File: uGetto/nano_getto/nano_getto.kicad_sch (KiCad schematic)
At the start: 9 parts, among them J1 Conn_01x06_Male, SW1 SW_Push, U1 ATtiny13A-SS

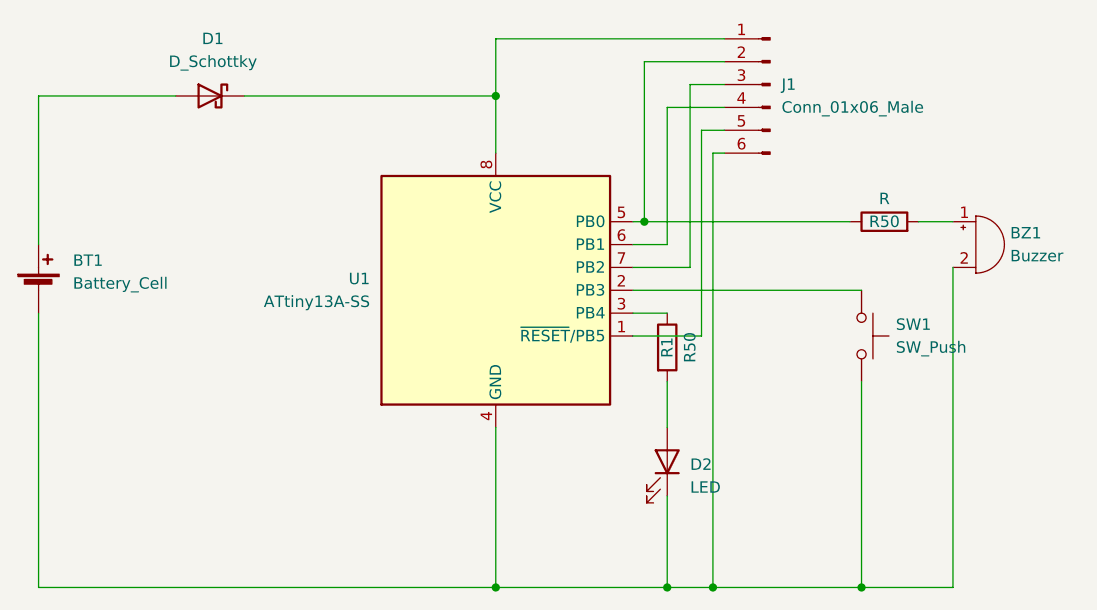
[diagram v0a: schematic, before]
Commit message: Changed attiny13a footprint to SOIC8W
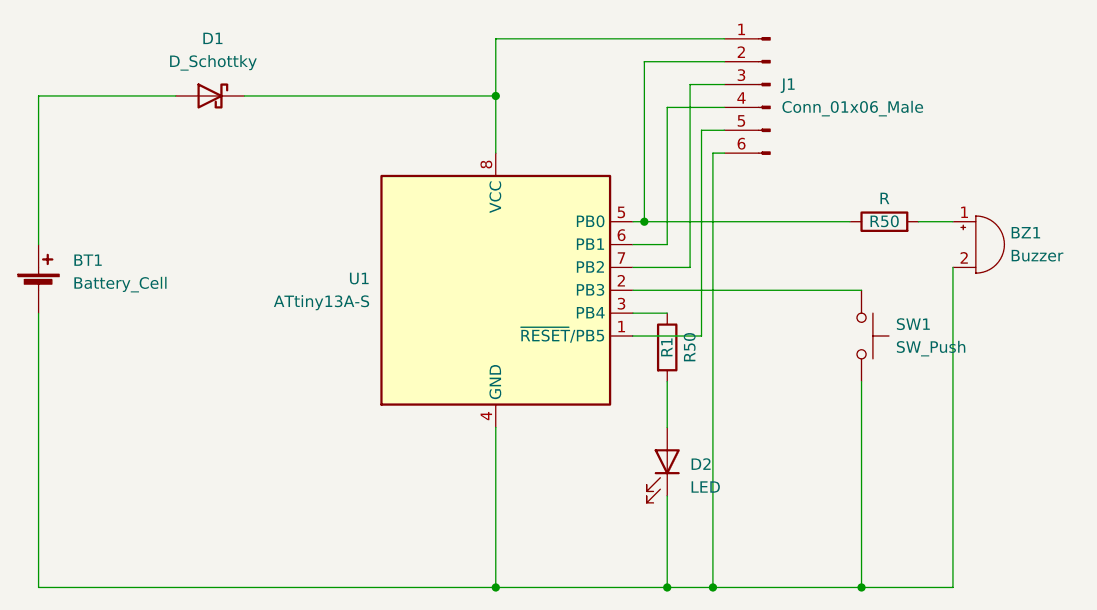
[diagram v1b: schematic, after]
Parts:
- removed U1: ATtiny13A-SS, Package_SO:SOIC-8_3.9x4.9mm_P1.27mm, symbol MCU_Microchip_ATtiny:ATtiny13A-SS
- added U1: ATtiny13A-S, Package_SO:SOIC-8W_5.3x5.3mm_P1.27mm, symbol MCU_Microchip_ATtiny:ATtiny13A-S
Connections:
- net at BT1.2 (-), BZ1.2 (+), D2.1 (K)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: now also U1.4 (GND)
- net at R1.1: now also U1.3 (PB4)
- net at D1.1 (K), J1.1 (Pin_1): now also U1.8 (VCC)
- net at J1.2 (Pin_2), R50.1: now also U1.5 (PB0)
- net at J1.3 (Pin_3): now also U1.7 (PB2)
- net at J1.4 (Pin_4): now also U1.6 (PB1)
- net at J1.5 (Pin_5): now also U1.1 (~{RESET}/PB5)
- net at SW1.1: now also U1.2 (PB3)
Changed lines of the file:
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@@
     (pin "2")
+  )
+  (symbol (lib_id "MCU_Microchip_ATtiny:ATtiny13A-S") (at 116.84 78.74 0) (unit 1)
+    (in_bom yes) (on_board yes) (fields_autoplaced)
+    (property "Reference" "U1" (id 0) (at 102.87 77.4699 0)
+      (effects (font (size 1.27 1.27)) (justify right))
+    )
+    (property "Value" "ATtiny13A-S" (id 1) (at 102.87 80.0099 0)
+      (effects (font (size 1.27 1.27)) (justify right))
+    )
+    (property "Footprint" "Package_SO:SOIC-8W_5.3x5.3mm_P1.27mm" (id 2) (at 116.84 78.74 0)
+      (effects (font (size 1.27 1.27) italic) hide)
+    )
+    (property "Datasheet" "http://ww1.microchip.com/downloads/en/DeviceDoc/doc8126.pdf" (id 3) (at 116.84 78.74 0)
+      (effects (font (size 1.27 1.27)) hide)
+    )
+    (pin "1")
+    (pin "2")
+    (pin "3")
+    (pin "4")
+    (pin "5")
+    (pin "6")
+    (pin "7")
+    (pin "8")
   )
   (symbol (lib_id "Device:LED") (at 135.89 97.79 270) (mirror x) (unit 1)
@@
     (pin "5")
     (pin "6")
-  )
-  (symbol (lib_id "MCU_Microchip_ATtiny:ATtiny13A-SS") (at 116.84 78.74 0) (unit 1)
-    (in_bom yes) (on_board yes) (fields_autoplaced)
-    (property "Reference" "U1" (id 0) (at 102.87 77.4699 0)
-      (effects (font (size 1.27 1.27)) (justify right))
-    )
-    (property "Value" "ATtiny13A-SS" (id 1) (at 102.87 80.0099 0)
-      (effects (font (size 1.27 1.27)) (justify right))
-    )
-    (property "Footprint" "Package_SO:SOIC-8_3.9x4.9mm_P1.27mm" (id 2) (at 116.84 78.74 0)
-      (effects (font (size 1.27 1.27) italic) hide)
-    )
-    (property "Datasheet" "http://ww1.microchip.com/downloads/en/DeviceDoc/doc8126.pdf" (id 3) (at 116.84 78.74 0)
-      (effects (font (size 1.27 1.27)) hide)
-    )
-    (pin "1")
-    (pin "2")
-    (pin "3")
-    (pin "4")
-    (pin "5")
-    (pin "6")
-    (pin "7")
-    (pin "8")
   )
   (symbol (lib_id "Device:Buzzer") (at 170.18 73.66 0) (unit 1)
@@
       (reference "SW1") (unit 1) (value "SW_Push") (footprint "Library:gomb")
     )
-    (path "/71c22f09-1c50-4481-a775-b5819b928cb3"
-      (reference "U1") (unit 1) (value "ATtiny13A-SS") (footprint "Package_SO:SOIC-8_3.9x4.9mm_P1.27mm")
+    (path "/1657004e-3e3e-49fb-8981-aed38f47dc7d"
+      (reference "U1") (unit 1) (value "ATtiny13A-S") (footprint "Package_SO:SOIC-8W_5.3x5.3mm_P1.27mm")
     )
   )
